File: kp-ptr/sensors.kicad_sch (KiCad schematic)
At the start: 36 parts

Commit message: GPS Signed-off-by: kretu <krecik@gmail.com>
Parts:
- removed U?: CAM-M8Q-0, LCC100P960X1400X210-31N, symbol KP-PTR_lib:CAM-M8Q-0
- added C?: 4.7uF, symbol Device:C
- added R?: 220, symbol Device:R
- added R?: 10k, symbol Device:R
- added R? (x2): 0 dla ublox, symbol Device:R
- added R?: 0 dla L96, symbol Device:R
- added U?: L96-M33, XCVR_L96-M33, symbol KP-PTR_lib:L96-M33
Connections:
- net +3V3: now also C?.1, R?.1, U?.8 (V_BCKP), U?.9 (VCC)
- net Earth: now also C?.2, R?.1
- new net: R?.1, U?.25 (TXD1)
- new net: R?.2, U?.1 (NC)
- new net: U?.10 (GND), U?.11 (GND), U?.12 (GND), U?.13 (GND), U?.14 (GND), U?.15 (GND), U?.18 (GND), U?.19 (GND), U?.21 (GND), U?.22 (GND), U?.27 (GND), U?.31 (GND), U?.4 (GND), U?.5 (GND)
- new net: R?.2, U?.2 (3D_FIX)
- new net: R?.2, U?.29 (TIMEPULSE)
- new net LED3: R?.1, R?.1
- new net U0RXD: R?.2
- new net U0TXD: R?.2, U?.26 (RXD1)
- no-connect marks 13 -> 14

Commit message: Footprints IN IMU9DOF OUT Signed-off-by: kretu <krecik@gmail.com>
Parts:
- removed C? (x3): 0.1uF, symbol Device:C
- removed D?: 1N4148, Diode_THT:D_DO-35_SOD27_P7.62mm_Horizontal, symbol Diode:1N4148
- removed Q? (x4): BSS138, Package_TO_SOT_SMD:SOT-23, symbol Transistor_FET:BSS138
- removed R? (x4): 4.7k, symbol Device:R
- removed R? (x5): 10k, symbol Device:R
- removed R?: 0, symbol Device:R
- removed U?: MPU-9250, Sensor_Motion:InvenSense_QFN-24_3x3mm_P0.4mm, symbol Sensor_Motion:MPU-9250
- C20, C21, C22, C23, C24, C25, C26, C27, C28, C29, C30: renamed from C?; footprint (none) -> Capacitor_SMD:C_01005_0402Metric_Pad0.57x0.30mm_HandSolder
- R17, R18, R19, R20: renamed from R?; footprint (none) -> Resistor_SMD:R_0402_1005Metric_Pad0.72x0.64mm_HandSolder
- R21, R23: renamed from R?; value 0 dla ublox -> DNP 0 dla ublox; footprint (none) -> Resistor_SMD:R_0402_1005Metric_Pad0.72x0.64mm_HandSolder
- R22: renamed from R?; value 0 dla L96 -> DNP 0 dla L96; footprint (none) -> Resistor_SMD:R_0402_1005Metric_Pad0.72x0.64mm_HandSolder
- U3: renamed from U?; footprint SON125P300X500X100-8N -> KP-PTR_lib:MS5607
- U4: renamed from U?; footprint PQFN50P300X300X100-16N -> KP-PTR_lib:MMC5983MA
- U5: renamed from U?; footprint LGA-16-3X3 -> KP-PTR_lib:LIS331
- U6: renamed from U?; footprint XCVR_L96-M33 -> KP-PTR_lib:XCVR_L96-M33
- U7: renamed from U?; footprint (none) -> KP-PTR_lib:LSM6DSO32
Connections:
- no-connect marks 14 -> 12
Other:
- note removed: "Do zastanowanie czy potrzebujemy INT z czujnika."
- note removed: "IMU 9DOF"
- note removed: "rezystor dla 9250 NC dla 20948"
- note removed: "założyłem że nie używamy Fsync"

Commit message: First sight of pcb Signed-off-by: kretu <krecik@gmail.com>
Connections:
- net Earth: now also U6.10 (GND), U6.11 (GND), U6.12 (GND), U6.13 (GND), U6.14 (GND), U6.15 (GND), U6.18 (GND), U6.19 (GND), U6.21 (GND), U6.22 (GND), U6.27 (GND), U6.31 (GND), U6.4 (GND), U6.5 (GND)
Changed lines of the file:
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@@
+    (stroke (width 0) (type default) (color 0 0 0 0))
+  )
+  (wire (pts (xy 187.96 148.59) (xy 182.88 148.59))
     (stroke (width 0) (type default) (color 0 0 0 0))
   )
@@
       (effects (font (size 1.27 1.27)) hide)
     )
+    (pin "1")
+  )
+  (symbol (lib_id "power:Earth") (at 187.96 148.59 0) (unit 1)
+    (in_bom yes) (on_board yes) (fields_autoplaced)
+    (property "Reference" "#PWR?" (id 0) (at 187.96 154.94 0)
+      (effects (font (size 1.27 1.27)) hide)
+    )
+    (property "Value" "Earth" (id 1) (at 187.96 152.4 0)
+      (effects (font (size 1.27 1.27)) hide)
+    )
+    (property "Footprint" "" (id 2) (at 187.96 148.59 0)
+      (effects (font (size 1.27 1.27)) hide)
+    )
+    (property "Datasheet" "~" (id 3) (at 187.96 148.59 0)
+      (effects (font (size 1.27 1.27)) hide)
+    )

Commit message: RF added, multiple small changes
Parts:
- added C?: 100n, Capacitor_SMD:C_01005_0402Metric_Pad0.57x0.30mm_HandSolder, symbol Device:C
- added C?: 47p, Capacitor_SMD:C_01005_0402Metric_Pad0.57x0.30mm_HandSolder, symbol Device:C
- added C?: DNP, Capacitor_SMD:C_01005_0402Metric_Pad0.57x0.30mm_HandSolder, symbol Device:C
- added C?: 100nF, Capacitor_SMD:C_01005_0402Metric_Pad0.57x0.30mm_HandSolder, symbol Device:C
- added D?: TBD, symbol Diode:ESD9B3.3ST5G
- added J?: u.fl, symbol Connector:Conn_Coaxial
- added L?: 27nH, symbol Device:L
- added R?: 10R, Resistor_SMD:R_0402_1005Metric_Pad0.72x0.64mm_HandSolder, symbol Device:R
- added R? (x2): 10k, Resistor_SMD:R_0402_1005Metric_Pad0.72x0.64mm_HandSolder, symbol Device:R
- R21, R23: value DNP 0 dla ublox -> DNP
- R22: value DNP 0 dla L96 -> 0R
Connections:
- net +3V3: now also R18.1, C?.1, R?.1, R?.1, R?.1
- net Earth: now also C?.2, C?.2, D?.1 (A1), J?.2 (Ext); no longer R18.1
- net SPI_CS_LSM: now also R?.2
- net SPI_CS_MAG: now also R?.2
- net at U6.16 (RF_OUT): now also C?.1, C?.1
- net at U6.17 (RF_IN): now also C?.2
- new net: C?.1, L?.1, R?.2
- new net: C?.2, J?.1 (In), L?.2
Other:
- note added: "L96: R21 - DNP R22 - 0R R23 - DNP ublox: R21 - DNP R22 - DNP R23 - 0R"
- moved on the sheet: C21, C26, C27, R23

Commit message: Weryfikacja footprintow faza I Signed-off-by: kretu <krecik@gmail.com>
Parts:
- removed R21: DNP, Resistor_SMD:R_0402_1005Metric_Pad0.72x0.64mm_HandSolder, symbol Device:R
- removed R22: 0R, Resistor_SMD:R_0402_1005Metric_Pad0.72x0.64mm_HandSolder, symbol Device:R
- added L5: 10nH, symbol Device:L
- added U9: NJG1156PCD, KP-PTR_lib:SON50P260X260X55-11N, symbol KP-PTR_lib:NJG1156PCD
- U6: value L96-M33 -> L76-L; footprint KP-PTR_lib:XCVR_L96-M33 -> XCVR_L76-L; symbol KP-PTR_lib:L96-M33 -> KP-PTR_lib:L76-L; MAXIMUM_PACKAGE_HEIGHT (none) -> 2.65mm; MF Quectel Wireless Solutions Co., Ltd -> Quectel; PARTREV (none) -> 3.1; STANDARD (none) -> Manufacturer Recommendations
- gave numbers to parts that had none: 10
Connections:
- net +3V3: no longer U6.8 (V_BCKP), U6.9 (VCC)
- net Earth: now also U6.1 (GND), U9.11 (GND), U9.6 (GND); no longer U6.11 (GND), U6.13 (GND), U6.14 (GND), U6.15 (GND), U6.18 (GND), U6.19 (GND), U6.21 (GND), U6.22 (GND), U6.27 (GND), U6.31 (GND), U6.4 (GND), U6.5 (GND)
- net U0TXD: no longer U6.26 (RXD1)
- net at R19.1: no longer U6.25 (TXD1)
- net at R23.2: now also U6.8 (VCC); no longer U6.1 (NC)
- net at C18.1, C19.1: no longer U6.16 (RF_OUT)
- net at U6.17 (NC): no longer C18.2
- new net: U6.13 (ANTON), U9.2 (Vctl)
- new net: L5.1, U9.8 (LNAIN)
- new net: L5.2, U9.7 (Pre/OUT)
- no-connect marks 12 -> 5

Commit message: Footprinty drobnicy
Signed-off-by: kretu <krecik@gmail.com>
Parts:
- C17, C18, C19, C20, C21, C22, C23, C24, C25, C26, C27, C28, C29, C30, C34: footprint Capacitor_SMD:C_01005_0402Metric_Pad0.57x0.30mm_HandSolder -> Capacitor_SMD:C_0402_1005Metric_Pad0.74x0.62mm_HandSolder
- U6: footprint XCVR_L76-L -> KP-PTR_lib:XCVR_L76-L
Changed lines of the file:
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@@
       (effects (font (size 1.27 1.27)) (justify left))
     )
-    (property "Footprint" "Capacitor_SMD:C_01005_0402Metric_Pad0.57x0.30mm_HandSolder" (id 2) (at 112.7252 78.74 0)
+    (property "Footprint" "Capacitor_SMD:C_0402_1005Metric_Pad0.74x0.62mm_HandSolder" (id 2) (at 112.7252 78.74 0)
       (effects (font (size 1.27 1.27)) hide)
     )
@@
       (effects (font (size 1.27 1.27)) (justify left))
     )
-    (property "Footprint" "Capacitor_SMD:C_01005_0402Metric_Pad0.57x0.30mm_HandSolder" (id 2) (at 116.5352 151.13 0)
+    (property "Footprint" "Capacitor_SMD:C_0402_1005Metric_Pad0.74x0.62mm_HandSolder" (id 2) (at 116.5352 151.13 0)
       (effects (font (size 1.27 1.27)) hide)
     )
@@
       (effects (font (size 1.27 1.27)) (justify left bottom))
     )
-    (property "Footprint" "XCVR_L76-L" (id 2) (at 160.02 130.81 0)
+    (property "Footprint" "KP-PTR_lib:XCVR_L76-L" (id 2) (at 160.02 130.81 0)
       (effects (font (size 1.27 1.27)) (justify left bottom) hide)
     )
@@
       (effects (font (size 1.27 1.27)) (justify left))
     )
-    (property "Footprint" "Capacitor_SMD:C_01005_0402Metric_Pad0.57x0.30mm_HandSolder" (id 2) (at 143.2052 78.74 0)
+    (property "Footprint" "Capacitor_SMD:C_0402_1005Metric_Pad0.74x0.62mm_HandSolder" (id 2) (at 143.2052 78.74 0)
       (effects (font (size 1.27 1.27)) hide)
     )
@@
       (effects (font (size 1.27 1.27)) (justify left))
     )
-    (property "Footprint" "Capacitor_SMD:C_01005_0402Metric_Pad0.57x0.30mm_HandSolder" (id 2) (at 55.5752 176.53 0)
+    (property "Footprint" "Capacitor_SMD:C_0402_1005Metric_Pad0.74x0.62mm_HandSolder" (id 2) (at 55.5752 176.53 0)
       (effects (font (size 1.27 1.27)) hide)
     )
@@
     (property "Reference" "C34" (id 0) (at 210.82 106.68 90))
     (property "Value" "100n" (id 1) (at 214.63 113.03 90))
-    (property "Footprint" "Capacitor_SMD:C_01005_0402Metric_Pad0.57x0.30mm_HandSolder" (id 2) (at 214.63 109.5248 0)
+    (property "Footprint" "Capacitor_SMD:C_0402_1005Metric_Pad0.74x0.62mm_HandSolder" (id 2) (at 214.63 109.5248 0)
       (effects (font (size 1.27 1.27)) hide)
     )
@@
       (effects (font (size 1.27 1.27)) (justify left))
     )
-    (property "Footprint" "Capacitor_SMD:C_01005_0402Metric_Pad0.57x0.30mm_HandSolder" (id 2) (at 187.6552 125.73 0)
+    (property "Footprint" "Capacitor_SMD:C_0402_1005Metric_Pad0.74x0.62mm_HandSolder" (id 2) (at 187.6552 125.73 0)
       (effects (font (size 1.27 1.27)) hide)
     )
@@
     (property "Reference" "C19" (id 0) (at 194.31 114.3 90))
     (property "Value" "DNP" (id 1) (at 194.31 121.92 90))
-    (property "Footprint" "Capacitor_SMD:C_01005_0402Metric_Pad0.57x0.30mm_HandSolder" (id 2) (at 198.12 117.1448 0)
+    (property "Footprint" "Capacitor_SMD:C_0402_1005Metric_Pad0.74x0.62mm_HandSolder" (id 2) (at 198.12 117.1448 0)
       (effects (font (size 1.27 1.27)) hide)
     )
@@
       (effects (font (size 1.27 1.27)) (justify left))
     )
-    (property "Footprint" "Capacitor_SMD:C_01005_0402Metric_Pad0.57x0.30mm_HandSolder" (id 2) (at 67.0052 176.53 0)
+    (property "Footprint" "Capacitor_SMD:C_0402_1005Metric_Pad0.74x0.62mm_HandSolder" (id 2) (at 67.0052 176.53 0)
       (effects (font (size 1.27 1.27)) hide)
     )
@@
       (effects (font (size 1.27 1.27)) (justify left))
     )
-    (property "Footprint" "Capacitor_SMD:C_01005_0402Metric_Pad0.57x0.30mm_HandSolder" (id 2) (at 237.1852 78.74 0)
+    (property "Footprint" "Capacitor_SMD:C_0402_1005Metric_Pad0.74x0.62mm_HandSolder" (id 2) (at 237.1852 78.74 0)
       (effects (font (size 1.27 1.27)) hide)
     )
@@
       (effects (font (size 1.27 1.27)) (justify left))
     )
-    (property "Footprint" "Capacitor_SMD:C_01005_0402Metric_Pad0.57x0.30mm_HandSolder" (id 2) (at 61.9252 77.47 0)
+    (property "Footprint" "Capacitor_SMD:C_0402_1005Metric_Pad0.74x0.62mm_HandSolder" (id 2) (at 61.9252 77.47 0)
       (effects (font (size 1.27 1.27)) hide)
     )
@@
       (effects (font (size 1.27 1.27)) (justify left))
     )
-    (property "Footprint" "Capacitor_SMD:C_01005_0402Metric_Pad0.57x0.30mm_HandSolder" (id 2) (at 251.1552 78.74 0)
+    (property "Footprint" "Capacitor_SMD:C_0402_1005Metric_Pad0.74x0.62mm_HandSolder" (id 2) (at 251.1552 78.74 0)
       (effects (font (size 1.27 1.27)) hide)
     )
@@
       (effects (font (size 1.27 1.27)) (justify left))
     )
-    (property "Footprint" "Capacitor_SMD:C_01005_0402Metric_Pad0.57x0.30mm_HandSolder" (id 2) (at 130.5052 151.13 0)
+    (property "Footprint" "Capacitor_SMD:C_0402_1005Metric_Pad0.74x0.62mm_HandSolder" (id 2) (at 130.5052 151.13 0)
       (effects (font (size 1.27 1.27)) hide)
     )
@@
       (effects (font (size 1.27 1.27)) (justify left))
     )
-    (property "Footprint" "Capacitor_SMD:C_01005_0402Metric_Pad0.57x0.30mm_HandSolder" (id 2) (at 37.7952 157.48 0)
+    (property "Footprint" "Capacitor_SMD:C_0402_1005Metric_Pad0.74x0.62mm_HandSolder" (id 2) (at 37.7952 157.48 0)
       (effects (font (size 1.27 1.27)) hide)
     )
@@
       (effects (font (size 1.27 1.27)) (justify left))
     )
-    (property "Footprint" "Capacitor_SMD:C_01005_0402Metric_Pad0.57x0.30mm_HandSolder" (id 2) (at 129.2352 78.74 0)
+    (property "Footprint" "Capacitor_SMD:C_0402_1005Metric_Pad0.74x0.62mm_HandSolder" (id 2) (at 129.2352 78.74 0)
       (effects (font (size 1.27 1.27)) hide)
     )
@@
       (effects (font (size 1.27 1.27)) (justify left))
     )
-    (property "Footprint" "Capacitor_SMD:C_01005_0402Metric_Pad0.57x0.30mm_HandSolder" (id 2) (at 220.6752 78.74 0)
-      (effects (font (size 1.27 1.27)) hide)
-    )
+    (property "Footprint" "Capacitor_SMD:C_0402_1005Metric_Pad0.74x0.62mm_HandSolder" (id 2) (at 220.6752 78.74 0)
+      (effects (font (size 1.27 1.27)) hide)
+    )

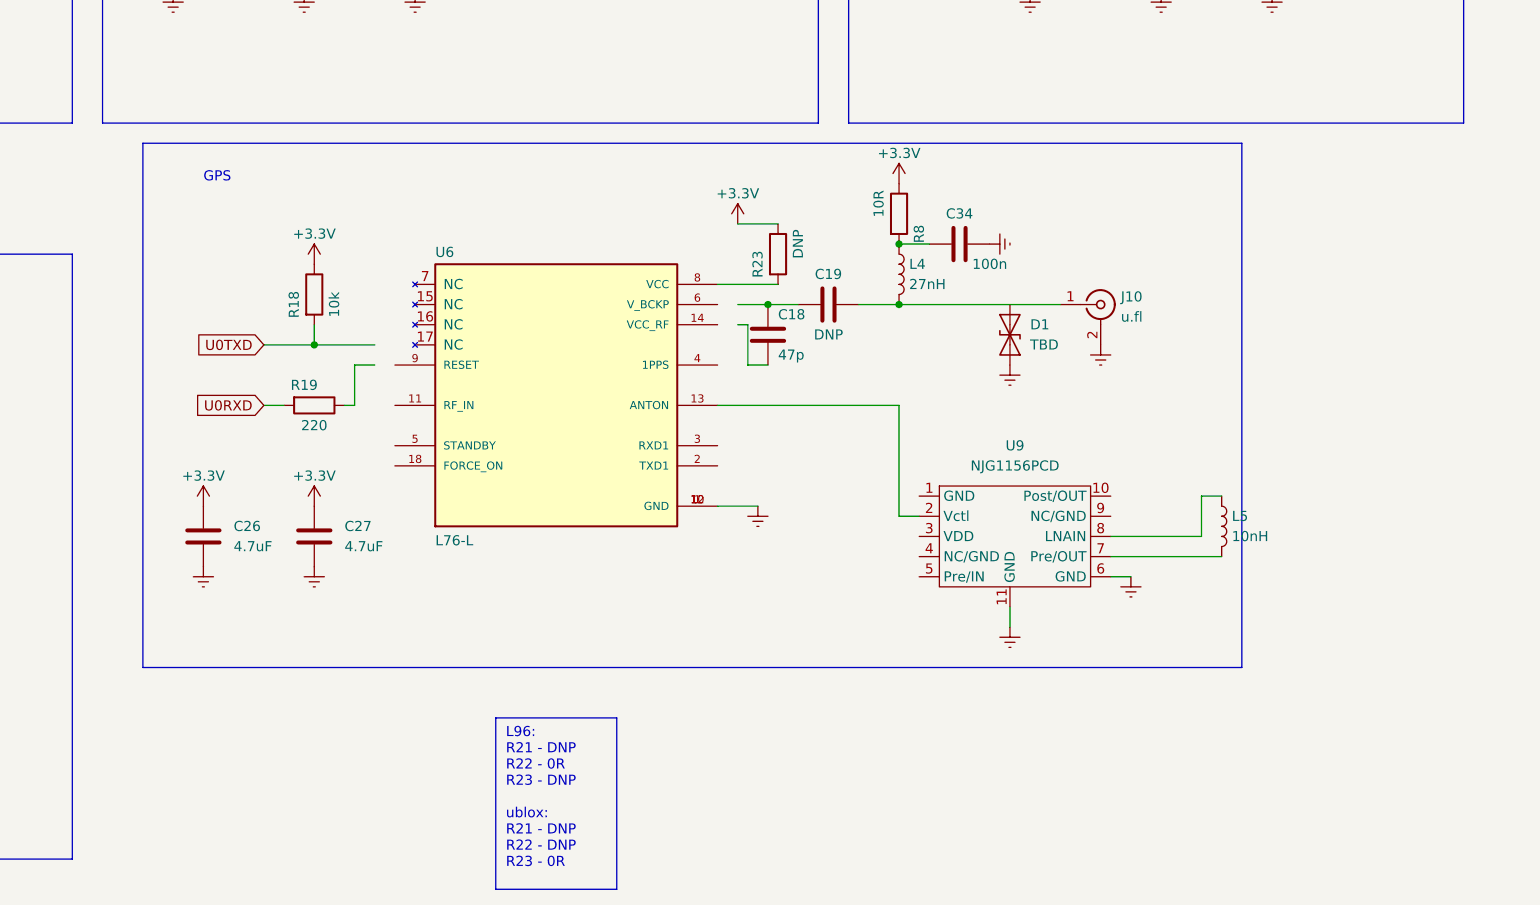
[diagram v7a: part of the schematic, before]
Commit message: Ogarnięty GPS i RF do anteny
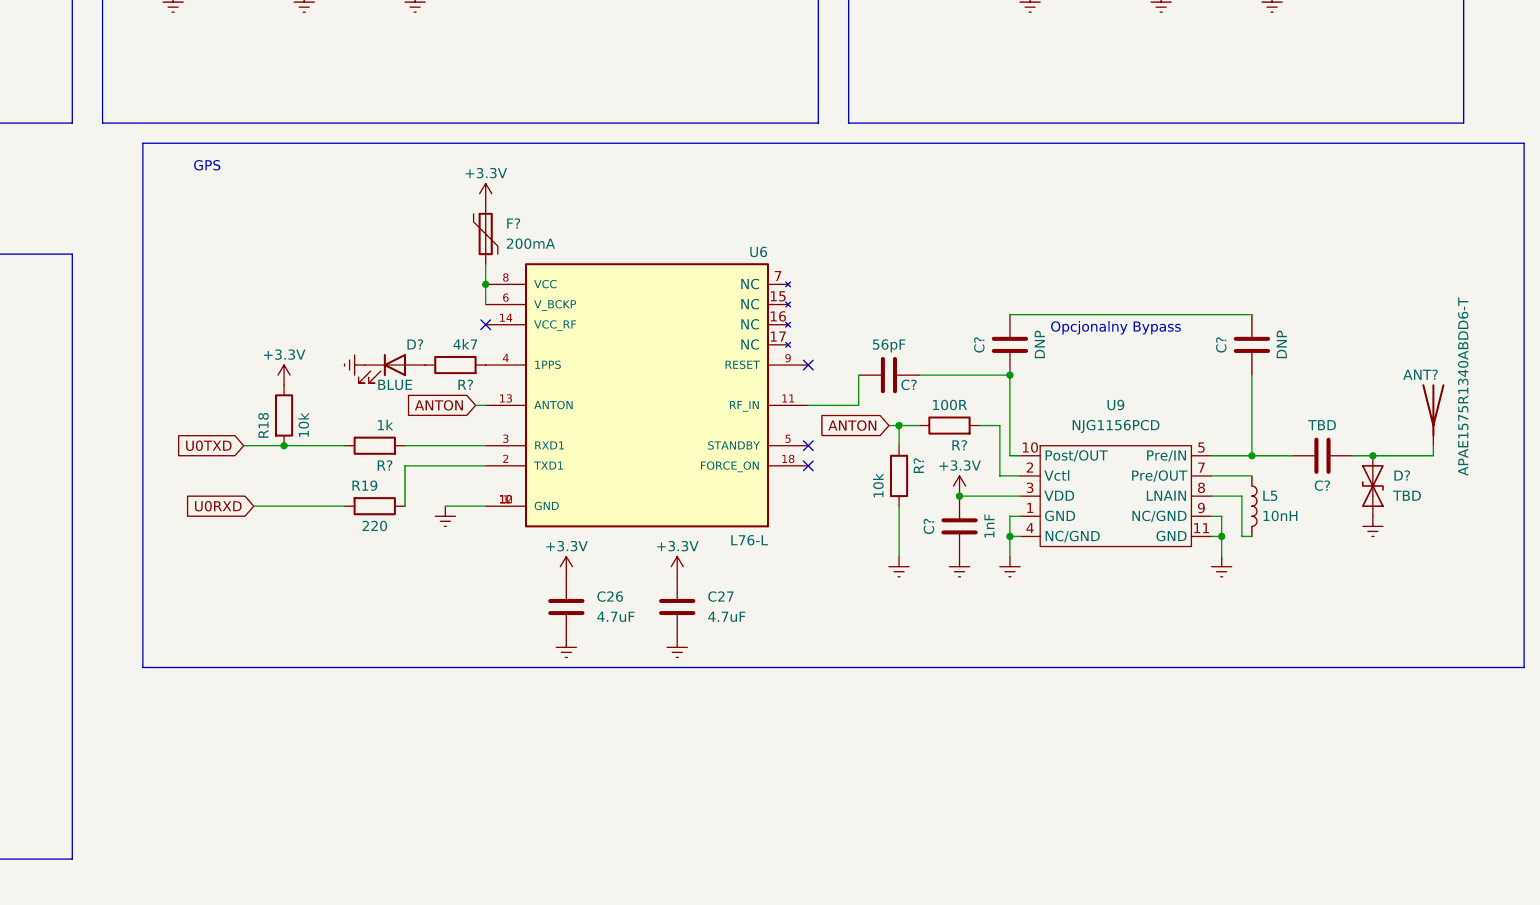
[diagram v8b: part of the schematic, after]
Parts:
- removed C18: 47p, Capacitor_SMD:C_0402_1005Metric_Pad0.74x0.62mm_HandSolder, symbol Device:C
- removed C19: DNP, Capacitor_SMD:C_0402_1005Metric_Pad0.74x0.62mm_HandSolder, symbol Device:C
- removed C34: 100n, Capacitor_SMD:C_0402_1005Metric_Pad0.74x0.62mm_HandSolder, symbol Device:C
- removed D1: TBD, symbol Diode:ESD9B3.3ST5G
- removed J10: u.fl, symbol Connector:Conn_Coaxial
- removed L4: 27nH, symbol Device:L
- removed R23: DNP, Resistor_SMD:R_0402_1005Metric_Pad0.72x0.64mm_HandSolder, symbol Device:R
- removed R8: 10R, Resistor_SMD:R_0402_1005Metric_Pad0.72x0.64mm_HandSolder, symbol Device:R
- added ANT?: APAE1575R1340ABDD6-T, symbol Device:Antenna
- added C?: TBD, Capacitor_SMD:C_0402_1005Metric_Pad0.74x0.62mm_HandSolder, symbol Device:C
- added C? (x2): DNP, Capacitor_SMD:C_0402_1005Metric_Pad0.74x0.62mm_HandSolder, symbol Device:C
- added C?: 56pF, Capacitor_SMD:C_0402_1005Metric_Pad0.74x0.62mm_HandSolder, symbol Device:C
- added C?: 1nF, Capacitor_SMD:C_0402_1005Metric_Pad0.74x0.62mm_HandSolder, symbol Device:C
- added D?: BLUE, LED_SMD:LED_0603_1608Metric_Pad1.05x0.95mm_HandSolder, symbol Device:LED
- added D?: TBD, symbol Diode:ESD9B3.3ST5G
- added F?: 200mA, symbol Device:Polyfuse
- added R?: 100R, Resistor_SMD:R_0402_1005Metric_Pad0.72x0.64mm_HandSolder, symbol Device:R
- added R?: 10k, Resistor_SMD:R_0402_1005Metric_Pad0.72x0.64mm_HandSolder, symbol Device:R
- added R?: 1k, Resistor_SMD:R_0402_1005Metric_Pad0.72x0.64mm_HandSolder, symbol Device:R
- added R?: 4k7, Resistor_SMD:R_0402_1005Metric_Pad0.72x0.64mm_HandSolder, symbol Device:R
- L5: footprint (none) -> Inductor_SMD:L_0402_1005Metric_Pad0.77x0.64mm_HandSolder
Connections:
- net +3V3: now also U9.3 (VDD), C?.2, F?.1
- net Earth: now also U9.1 (GND), U9.4 (NC/GND), U9.9 (NC/GND), C?.1, D?.1 (A1), D?.1 (K), R?.1; no longer U9.6 (GND)
- net U0TXD: now also R?.1
- net at R19.1: now also U6.2 (TXD1)
- net at U6.11 (RF_IN): now also C?.2
- net at U9.2 (Vctl): now also R?.2; no longer U6.13 (ANTON)
- net at U6.3 (RXD1): now also R?.2
- net at U6.4 (1PPS): now also R?.2
- net at U6.6 (V_BCKP): now also U6.8 (VCC), F?.2
- net at L5.1: now also U9.7 (Pre/OUT); no longer U9.8 (LNAIN)
- net at L5.2: now also U9.8 (LNAIN); no longer U9.7 (Pre/OUT)
- net at U9.10 (Post/OUT): now also C?.1, C?.1
- net at U9.5 (Pre/IN): now also C?.1, C?.2
- new net: ANT?.1 (A), C?.1, D?.2 (A2)
- new net: C?.2, C?.2
- new net: D?.2 (A), R?.1
- new net ANTON: R?.1, R?.2, U6.13 (ANTON)
- no-connect marks 5 -> 9
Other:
- note added: "Opcjonalny Bypass"
- note removed: "L96: R21 - DNP R22 - 0R R23 - DNP ublox: R21 - DNP R22 - DNP R23 - 0R"
- moved on the sheet: C26, C27, L5, R18, R19, U6
